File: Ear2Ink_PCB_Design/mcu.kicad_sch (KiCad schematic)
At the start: 35 parts, among them J1 Conn_02x16_Top_Bottom, J2 Conn_01x08_Pin, J3 Conn_01x08_Pin, J4 Micro_SD_Card_Det1, J5 Conn_01x06_Pin, J6 Conn_01x04_Pin, SW1 SW_Push, U1 STM32F411RETx, Y1 MAX7375AXR805

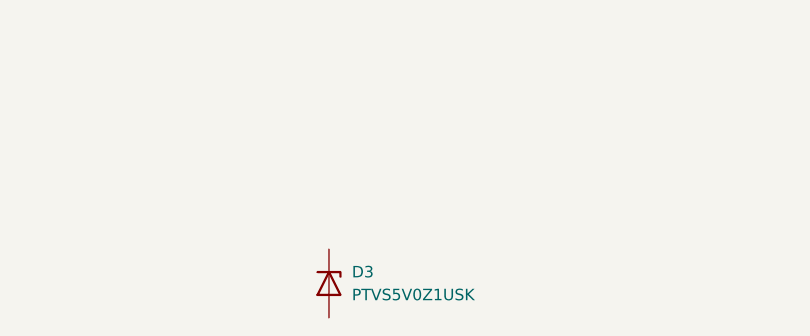
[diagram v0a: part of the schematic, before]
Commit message: working on erc errors
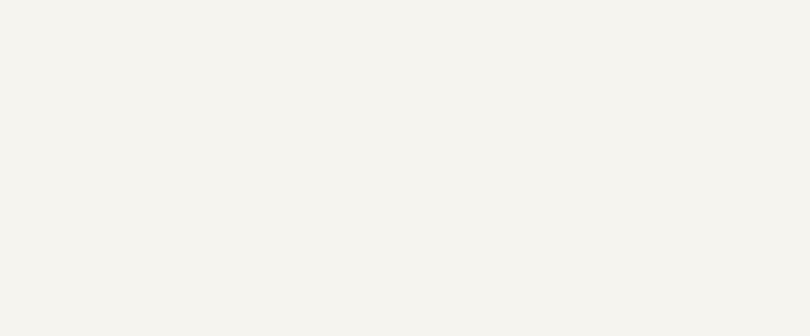
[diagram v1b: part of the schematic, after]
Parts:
- removed D3: PTVS5V0Z1USK, Diode_SMD:Nexperia_DSN1608-2_1.6x0.8mm, symbol Diode:PTVS5V0Z1USK
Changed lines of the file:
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@@
-	)
-	(symbol
-		(lib_id "Diode:PTVS5V0Z1USK")
-		(at 156.21 240.03 270)
-		(unit 1)
-		(exclude_from_sim no)
-		(in_bom yes)
-		(on_board yes)
-		(dnp no)
-		(fields_autoplaced yes)
-		(property "Reference" "D3"
-			(at 158.75 238.7599 90)
-			(effects
-				(font
-					(size 1.27 1.27)
-				)
-				(justify left)
-			)
-		)
-		(property "Value" "PTVS5V0Z1USK"
-			(at 158.75 241.2999 90)
-			(effects
-				(font
-					(size 1.27 1.27)
-				)
-				(justify left)
-			)
-		)
-		(property "Footprint" "Diode_SMD:Nexperia_DSN1608-2_1.6x0.8mm"
-			(at 151.765 240.03 0)
-			(effects
-				(font
-					(size 1.27 1.27)
-				)
-				(hide yes)
-			)
-		)
-		(property "Datasheet" "https://assets.nexperia.com/documents/data-sheet/PTVS5V0Z1USK.pdf"
-			(at 156.21 240.03 0)
-			(effects
-				(font
-					(size 1.27 1.27)
-				)
-				(hide yes)
-			)
-		)
-		(property "Description" "5V, 1200W TVS unidirectional diode, DSN1608-2"
-			(at 156.21 240.03 0)
-			(effects
-				(font
-					(size 1.27 1.27)
-				)
-				(hide yes)
-			)
-		)
-		(pin "1"
-		)
-		(pin "2"
-		)
-		(instances
-			(project ""
-				(path "/cdb6d8ac-bdfd-4608-bf70-aa82e76498ad/2ddad00a-af62-4659-9017-a3cd158a818d"
-					(reference "D3")
-					(unit 1)
-				)
-			)
-		)
 	)
 	(symbol

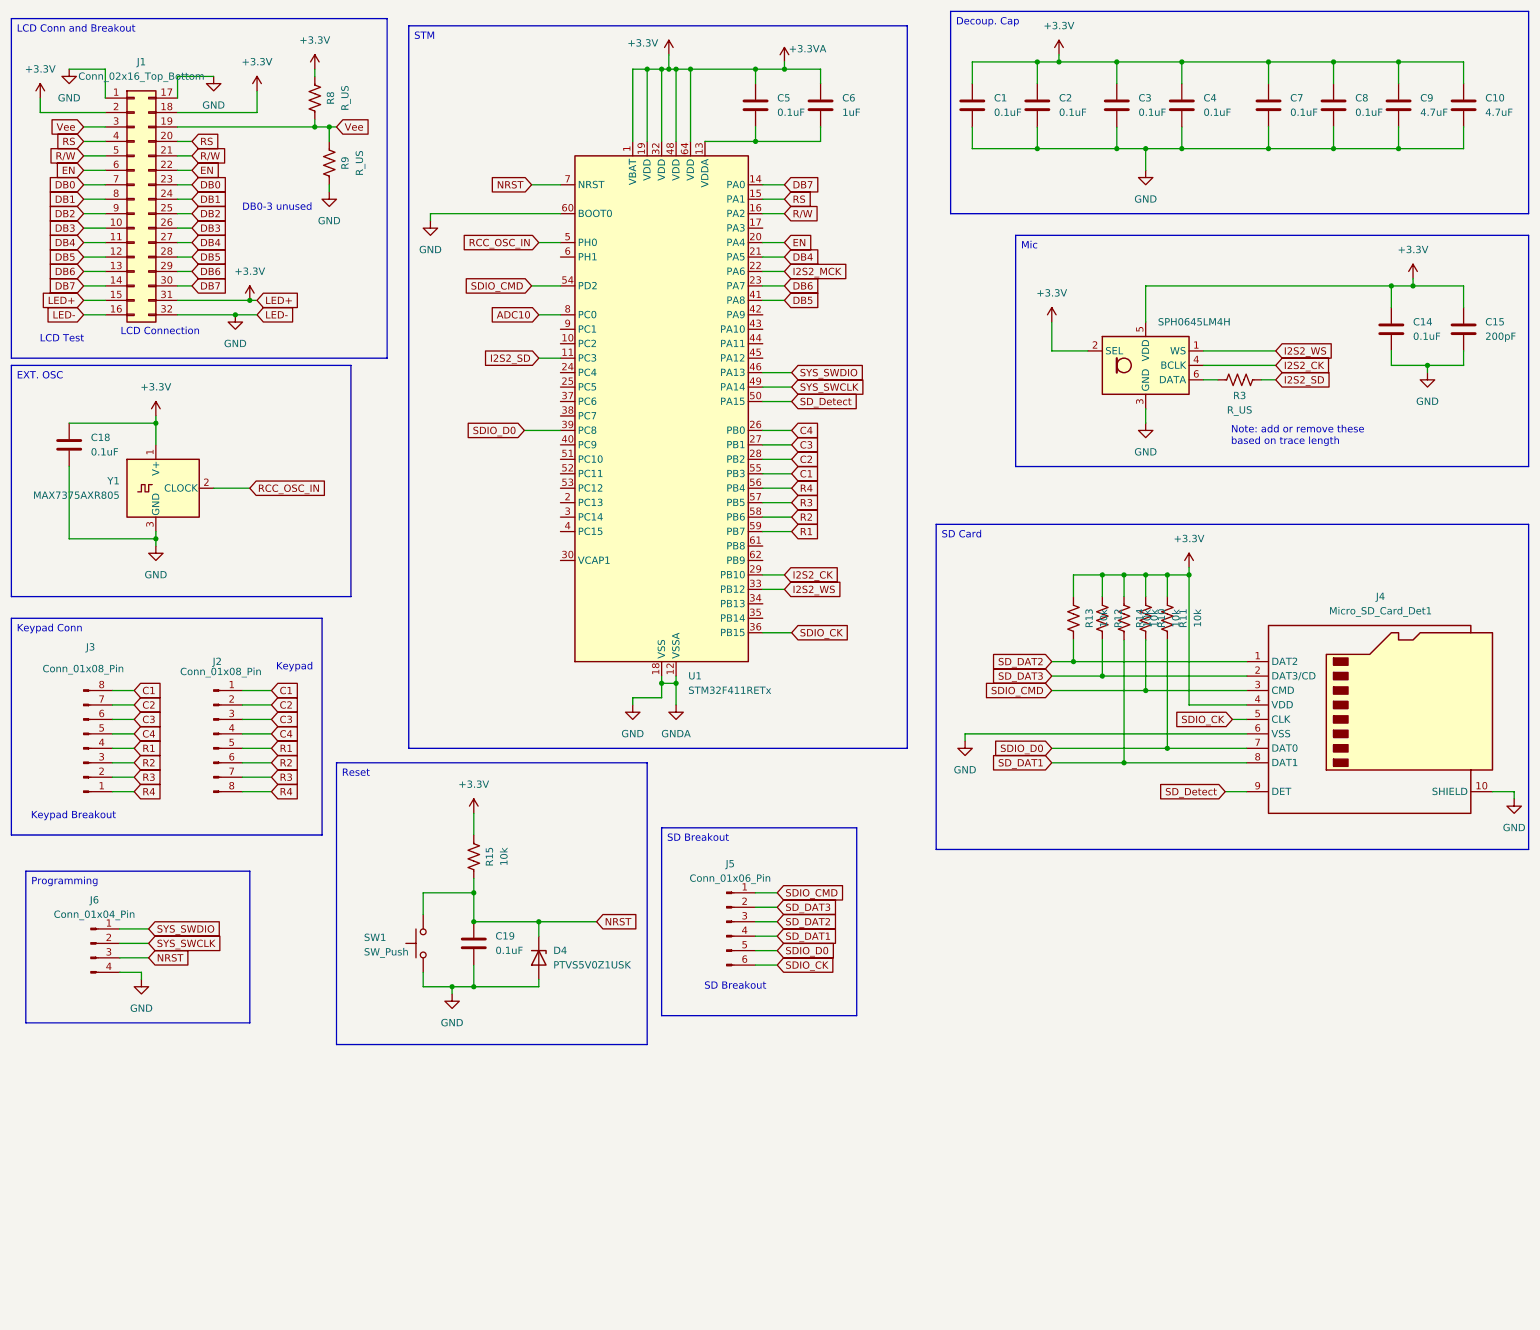
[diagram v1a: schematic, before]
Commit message: fixed erc stuff
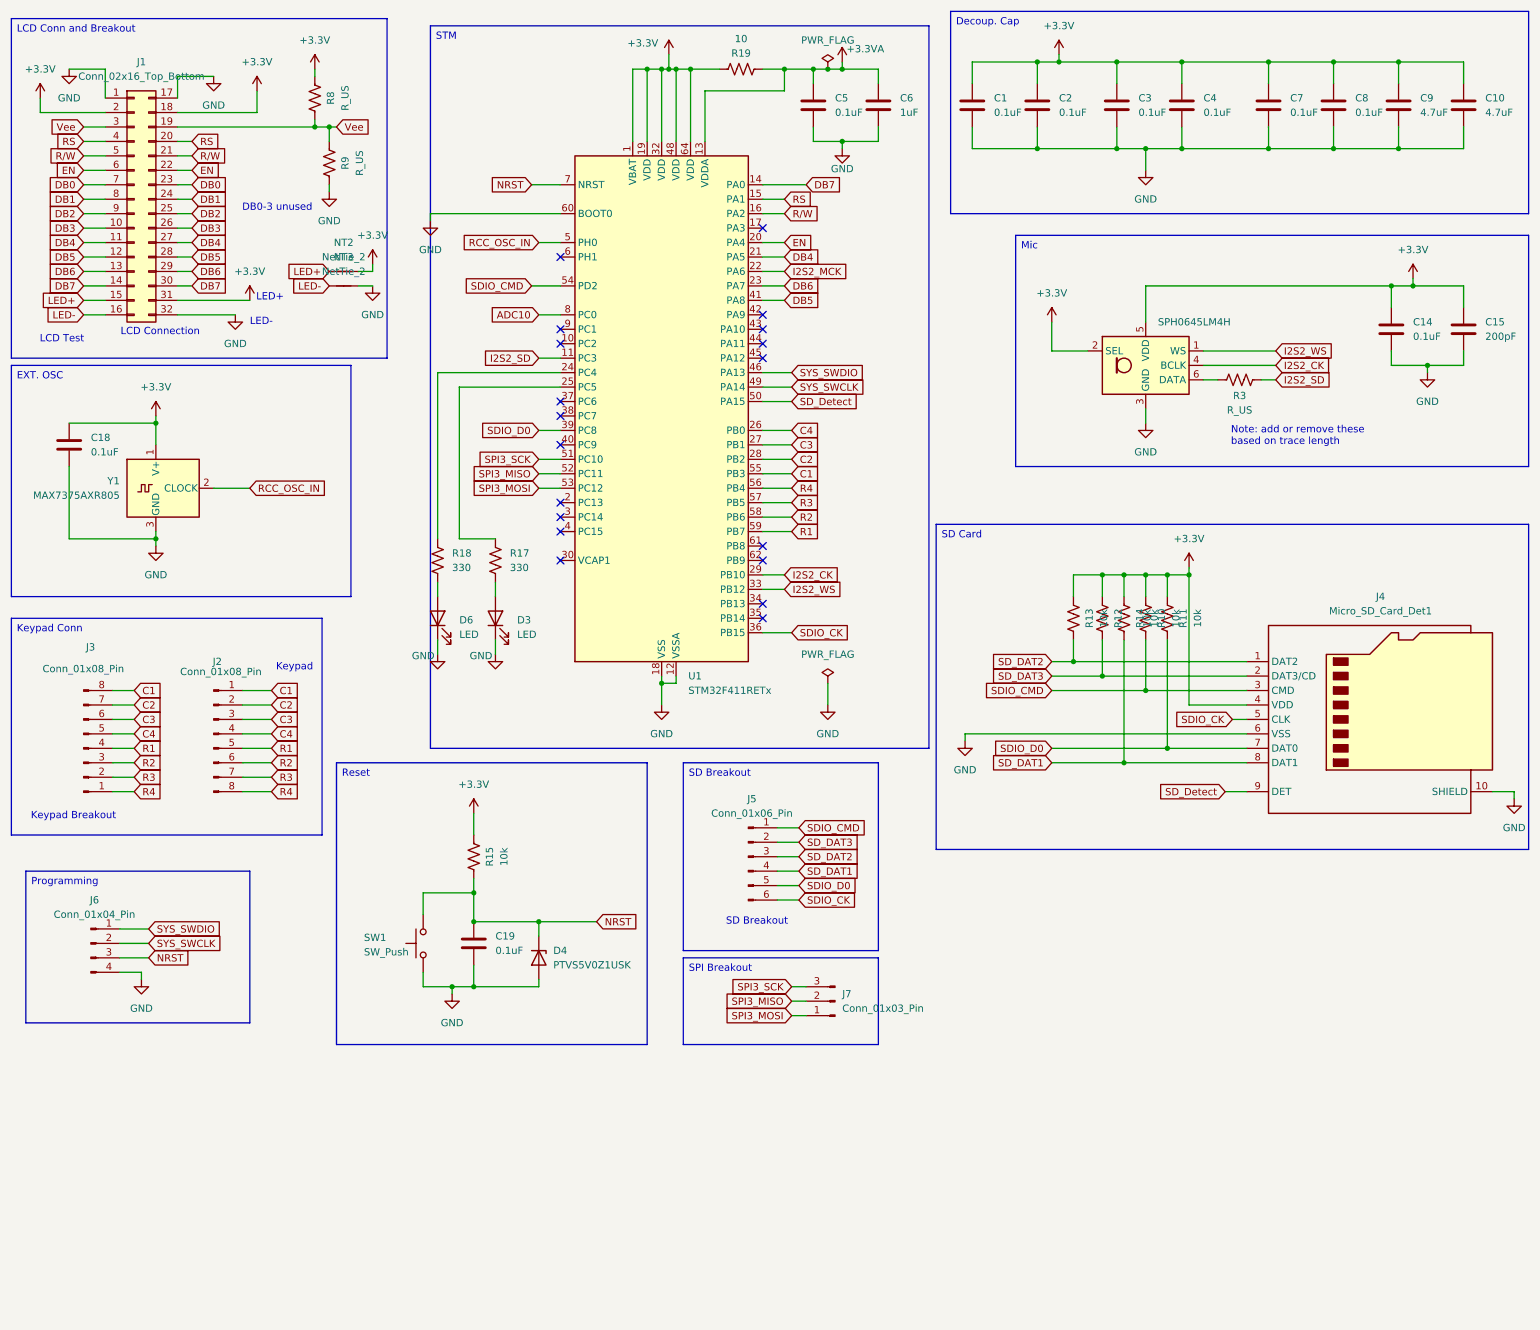
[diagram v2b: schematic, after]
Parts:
- added D3, D6: LED, Resistor_SMD:R_0805_2012Metric_Pad1.20x1.40mm_HandSolder, symbol Device:LED
- added J7: Conn_01x03_Pin, Connector_PinHeader_2.54mm:PinHeader_1x03_P2.54mm_Vertical, symbol Connector:Conn_01x03_Pin
- added NT2, NT3: NetTie_2, NetTie:NetTie-2_SMD_Pad0.5mm, symbol Device:NetTie_2
- added R17, R18: 330, Capacitor_SMD:C_0603_1608Metric_Pad1.08x0.95mm_HandSolder, symbol Device:R_US
- added R19: 10, Capacitor_SMD:C_0603_1608Metric_Pad1.08x0.95mm_HandSolder, symbol Device:R_US
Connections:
- net +3.3V: now also NT2.2, R19.1; no longer C5.1, C6.1, J1.15 (Pin_15)
- net GND: now also C5.2, C6.2, D3.1 (K), D6.1 (K), NT3.2; no longer J1.16 (Pin_16)
- net at U1.24 (PC4): now also R18.1
- net at U1.25 (PC5): now also R17.1
- net SPI3_SCK: now reaches U1.51 (PC10)
- net SPI3_SCK: now also J7.3 (Pin_3)
- net SPI3_MISO: now reaches U1.52 (PC11)
- net SPI3_MISO: now also J7.2 (Pin_2)
- net SPI3_MOSI: now reaches U1.53 (PC12)
- net SPI3_MOSI: now also J7.1 (Pin_1)
- new net: D6.2 (A), R18.2
- new net: D3.2 (A), R17.2
- new net +3.3VA: C5.1, C6.1, R19.2, U1.13 (VDDA)
- new net LED+: J1.15 (Pin_15), NT2.1
- new net LED-: J1.16 (Pin_16), NT3.1
- no-connect marks 0 -> 19
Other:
- note added: "LED+"
- note added: "LED-"
- moved on the sheet: C5, C6, J5

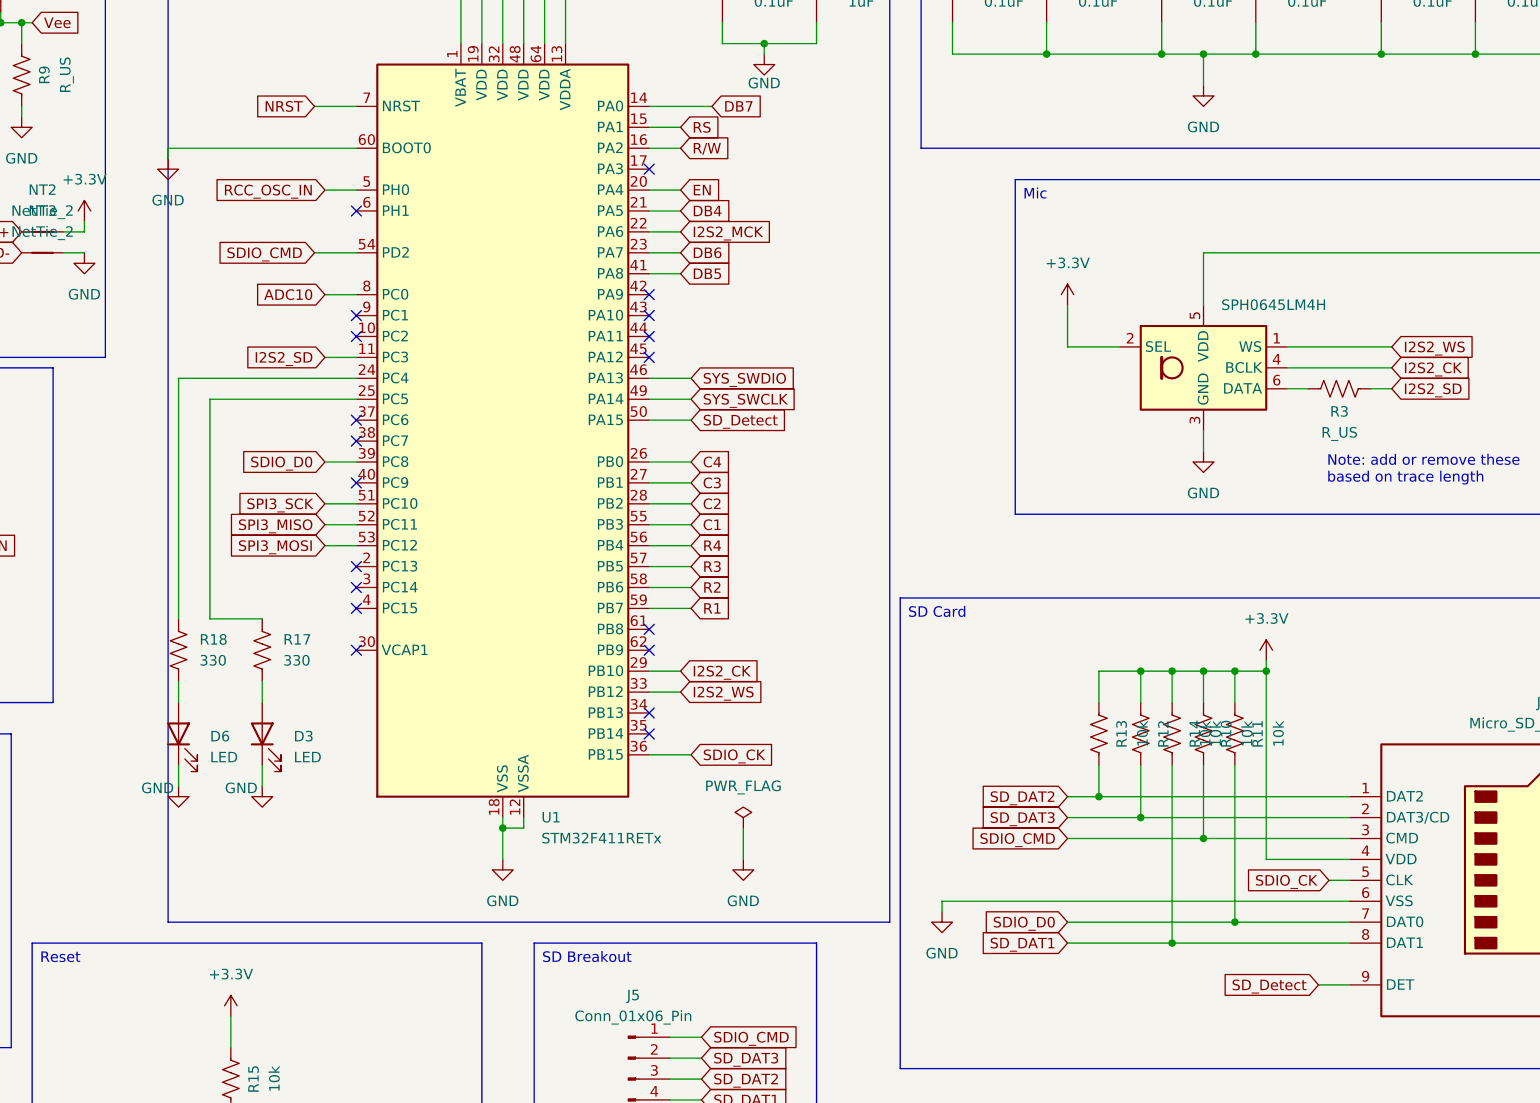
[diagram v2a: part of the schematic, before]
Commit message: SDIO to SPI
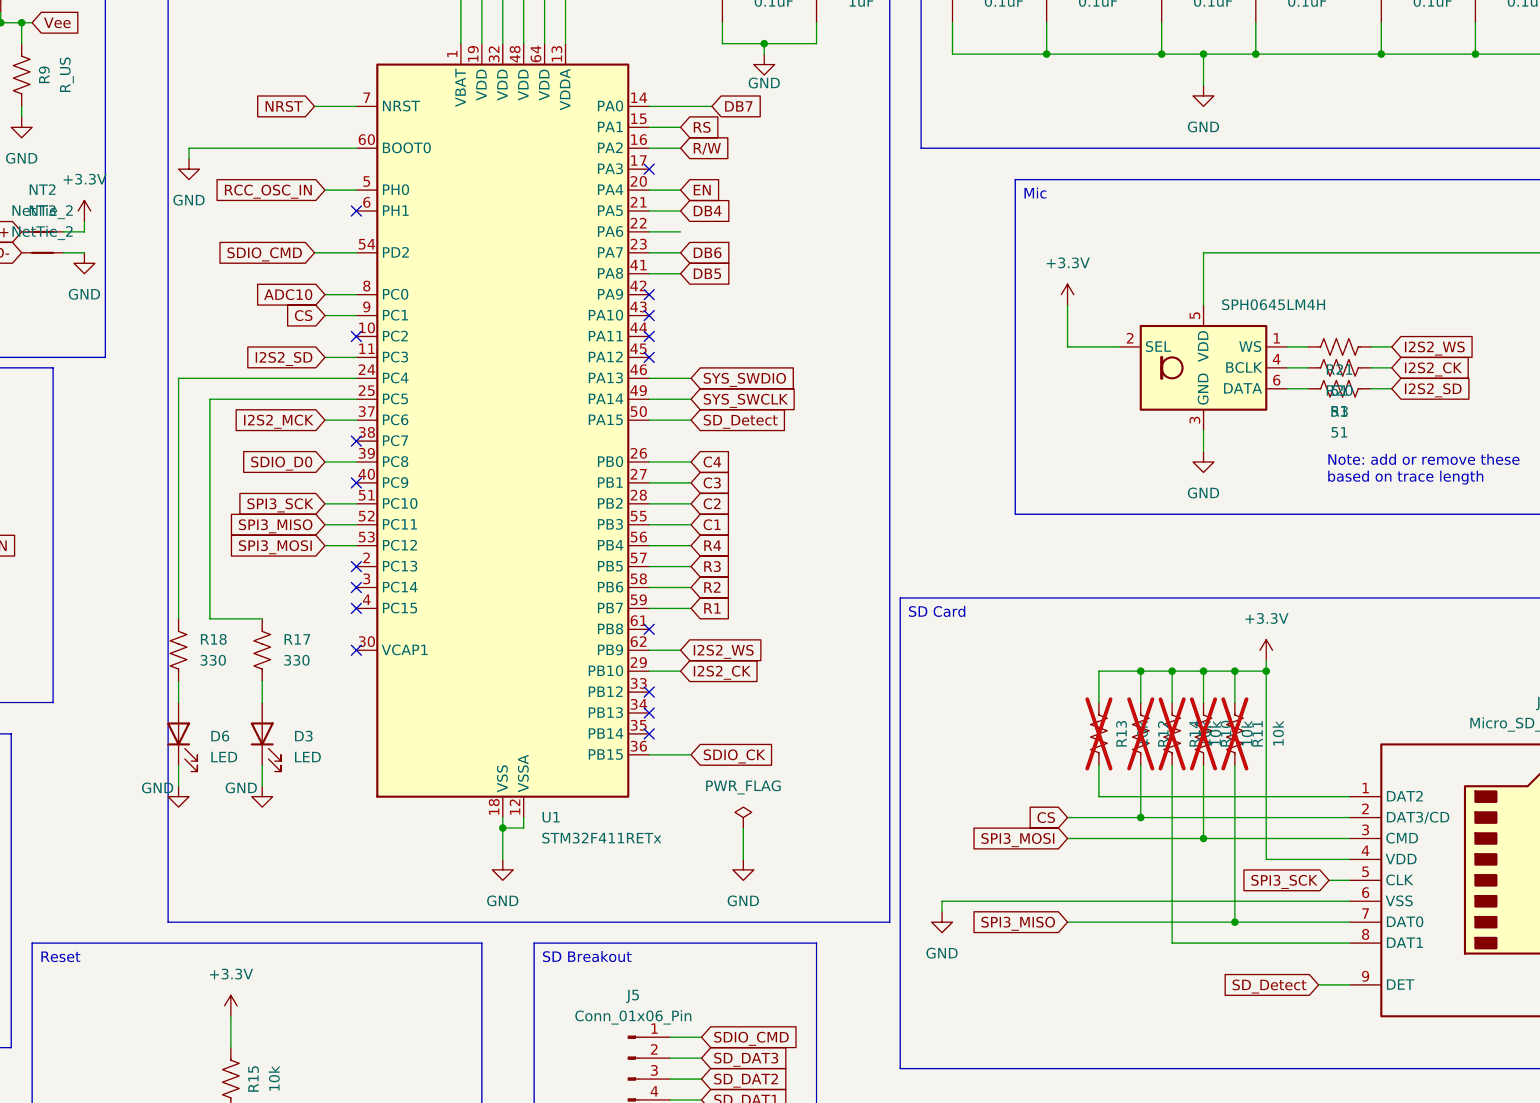
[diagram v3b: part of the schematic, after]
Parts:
- added R20, R21: 51, Resistor_SMD:R_0603_1608Metric_Pad0.98x0.95mm_HandSolder, symbol Device:R_US
- D3, D6: footprint Resistor_SMD:R_0805_2012Metric_Pad1.20x1.40mm_HandSolder -> LED_SMD:LED_0805_2012Metric_Pad1.15x1.40mm_HandSolder
- R10, R11, R12, R13, R14: footprint Capacitor_SMD:C_0603_1608Metric_Pad1.08x0.95mm_HandSolder -> Resistor_SMD:R_0603_1608Metric_Pad0.98x0.95mm_HandSolder; now not fitted
- R15, R17, R18, R19, R8, R9: footprint Capacitor_SMD:C_0603_1608Metric_Pad1.08x0.95mm_HandSolder -> Resistor_SMD:R_0603_1608Metric_Pad0.98x0.95mm_HandSolder
- R3: value R_US -> 51; footprint Capacitor_SMD:C_0603_1608Metric_Pad1.08x0.95mm_HandSolder -> Resistor_SMD:R_0603_1608Metric_Pad0.98x0.95mm_HandSolder
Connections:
- net I2S2_CK: now also R20.1; no longer MK1.4 (BCLK)
- net I2S2_MCK: now also U1.37 (PC6); no longer U1.22 (PA6)
- net I2S2_WS: now also U1.62 (PB9), R21.1; no longer MK1.1 (WS), U1.33 (PB12)
- net SDIO_CK: no longer J4.5 (CLK)
- net SDIO_CMD: no longer J4.3 (CMD), R10.2
- net SDIO_D0: no longer J4.7 (DAT0), R11.2
- net SD_DAT1: no longer J4.8 (DAT1), R14.2
- net SD_DAT2: no longer J4.1 (DAT2), R13.2
- net SD_DAT3: no longer J4.2 (DAT3/CD), R12.2
- net SPI3_MISO: now also J4.7 (DAT0), R11.2
- net SPI3_MOSI: now also J4.3 (CMD), R10.2
- net SPI3_SCK: now also J4.5 (CLK)
- net CS: now reaches U1.9 (PC1)
- net CS: now also J4.2 (DAT3/CD), R12.2
- new net: MK1.1 (WS), R21.2
- new net: MK1.4 (BCLK), R20.2
- new net: J4.8 (DAT1), R14.2
- new net: J4.1 (DAT2), R13.2
- no-connect marks 19 -> 17
